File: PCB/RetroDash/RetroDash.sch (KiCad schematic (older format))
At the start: 4 parts

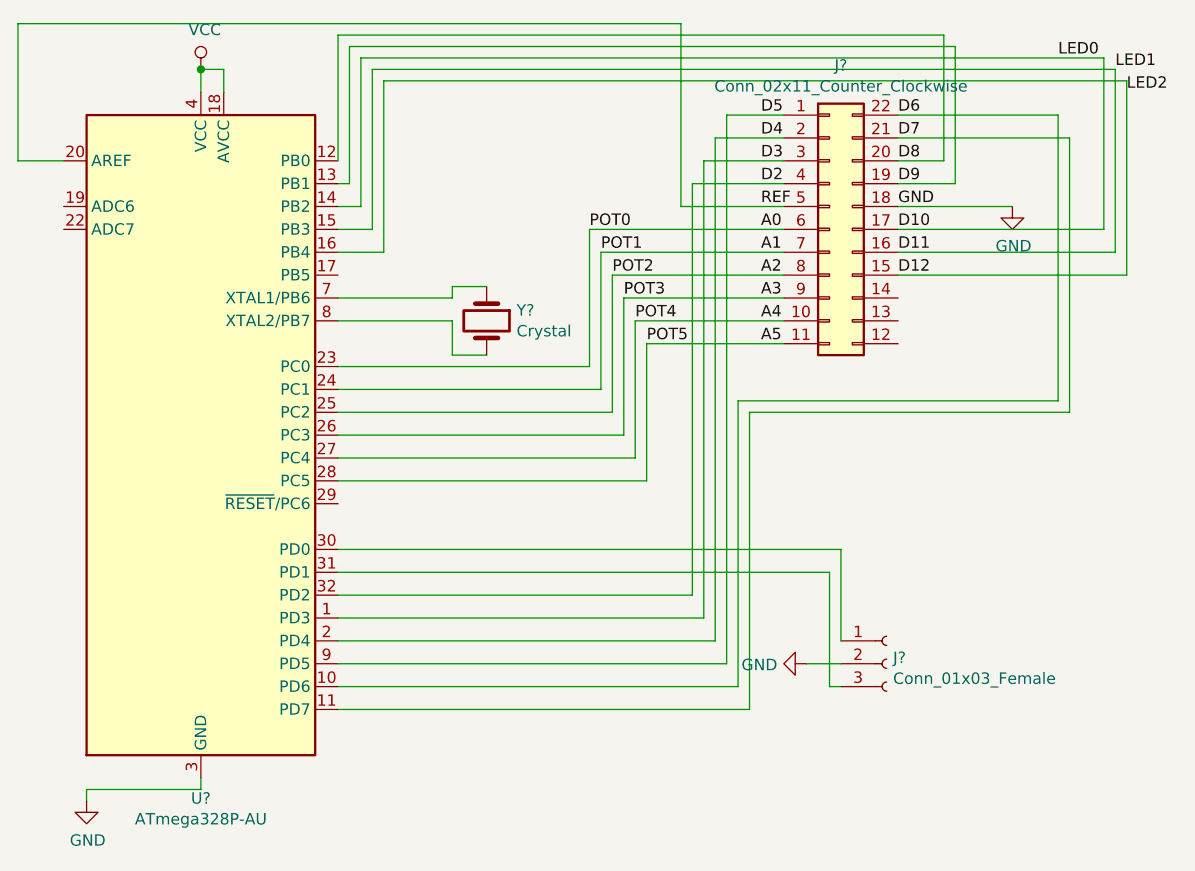
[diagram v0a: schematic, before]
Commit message: fixed nc pin
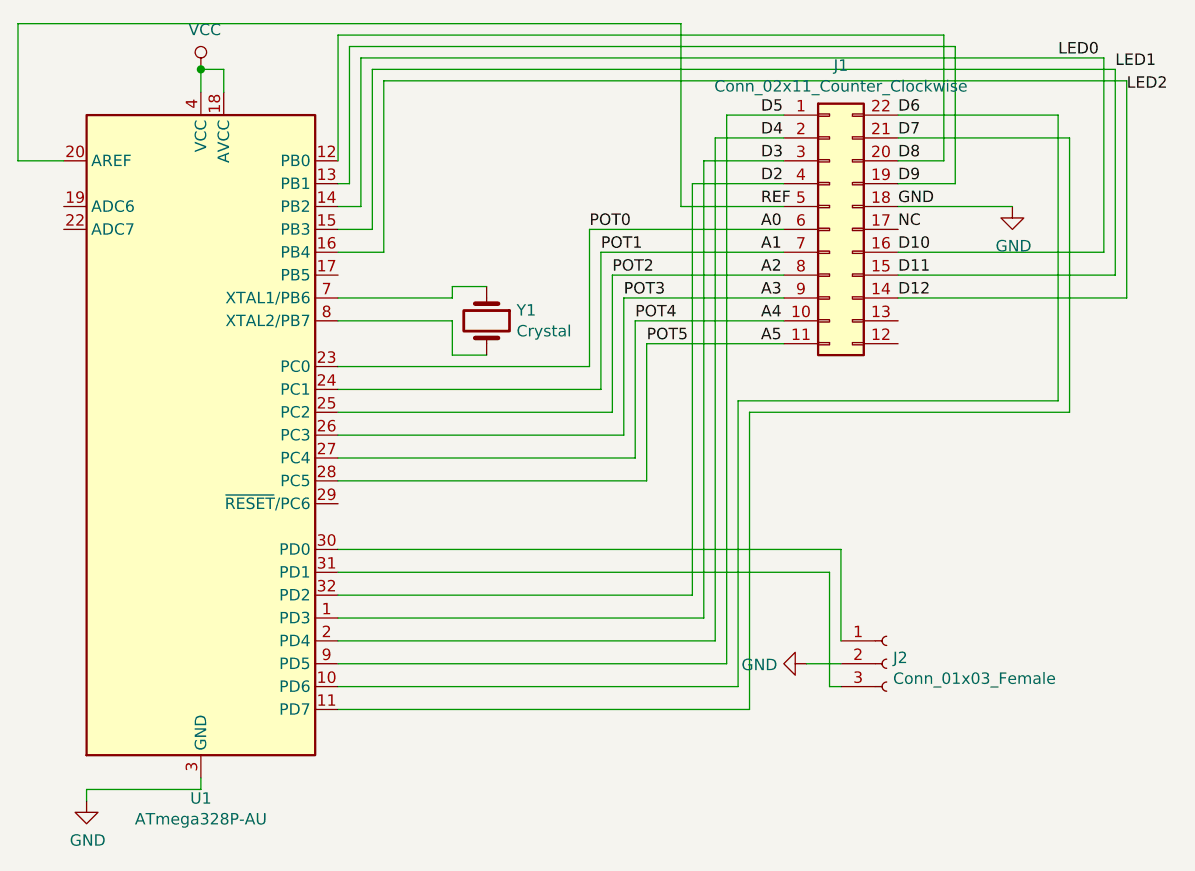
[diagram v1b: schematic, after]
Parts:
- gave numbers to parts that had none: 4
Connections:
- net D10: now also J1.16 (Pin_16); no longer J1.17 (Pin_17)
- net D11: now also J1.15 (Pin_15); no longer J1.16 (Pin_16)
- net D12: now also J1.14 (Pin_14); no longer J1.15 (Pin_15)
- new net NC: J1.17 (Pin_17)
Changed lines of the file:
@@
 EESchema Schematic File Version 4
+LIBS:RetroDash-cache
 EELAYER 29 0
 EELAYER END
@@
 $EndDescr
 $Comp
-L Connector_Generic:Conn_02x11_Counter_Clockwise J?
+L Connector_Generic:Conn_02x11_Counter_Clockwise J1
 U 1 1 5CB62158
 P 6600 1650
-F 0 "J?" H 6650 2367 50  0000 C CNN
+F 0 "J1" H 6650 2367 50  0000 C CNN
 F 1 "Conn_02x11_Counter_Clockwise" H 6650 2276 50  0000 C CNN
 F 2 "" H 6600 1650 50  0001 C CNN
@@
 	6900 1550 7400 1550
 $Comp
-L power:GND #PWR?
+L power:GND #PWR0101
 U 1 1 5CB6A467
 P 7400 1550
-F 0 "#PWR?" H 7400 1300 50  0001 C CNN
+F 0 "#PWR0101" H 7400 1300 50  0001 C CNN
 F 1 "GND" H 7405 1377 50  0000 C CNN
 F 2 "" H 7400 1550 50  0001 C CNN
@@
 $EndComp
 $Comp
-L power:GND #PWR?
+L power:GND #PWR0102
 U 1 1 5CB6B3B1
 P 3350 4150
-F 0 "#PWR?" H 3350 3900 50  0001 C CNN
+F 0 "#PWR0102" H 3350 3900 50  0001 C CNN
 F 1 "GND" H 3355 3977 50  0000 C CNN
 F 2 "" H 3350 4150 50  0001 C CNN
@@
 	5950 1550 6400 1550
 $Comp
-L power:VCC #PWR?
+L power:VCC #PWR0103
 U 1 1 5CB6F2DF
 P 3850 950
-F 0 "#PWR?" H 3850 800 50  0001 C CNN
+F 0 "#PWR0103" H 3850 800 50  0001 C CNN
 F 1 "VCC" H 3867 1123 50  0000 C CNN
 F 2 "" H 3850 950 50  0001 C CNN
@@
 	5800 2750 4450 2750
 $Comp
-L power:GND #PWR?
+L power:GND #PWR0104
 U 1 1 5CB77E47
 P 6500 3550
-F 0 "#PWR?" H 6500 3300 50  0001 C CNN
+F 0 "#PWR0104" H 6500 3300 50  0001 C CNN
 F 1 "GND" V 6505 3422 50  0000 R CNN
 F 2 "" H 6500 3550 50  0001 C CNN
@@
 	5950 750  5950 1550
 $Comp
-L Connector:Conn_01x03_Female J?
+L Connector:Conn_01x03_Female J2
 U 1 1 5CB74F2E
 P 6850 3550
-F 0 "J?" H 6878 3576 50  0000 L CNN
+F 0 "J2" H 6878 3576 50  0000 L CNN
 F 1 "Conn_01x03_Female" H 6878 3485 50  0000 L CNN
 F 2 "" H 6850 3550 50  0001 C CNN
@@
 $EndComp
 $Comp
-L Device:Crystal Y?
+L Device:Crystal Y1
 U 1 1 5CB70044
 P 5100 2050
-F 0 "Y?" V 5054 2181 50  0000 L CNN
+F 0 "Y1" V 5054 2181 50  0000 L CNN
 F 1 "Crystal" V 5145 2181 50  0000 L CNN
 F 2 "" H 5100 2050 50  0001 C CNN
@@
 	4450 1950 4950 1950
 $Comp
-L MCU_Microchip_ATmega:ATmega328P-AU U?
+L MCU_Microchip_ATmega:ATmega328P-AU U1
 U 1 1 5CB6371F
 P 3850 2550
-F 0 "U?" H 3850 961 50  0000 C CNN
+F 0 "U1" H 3850 961 50  0000 C CNN
 F 1 "ATmega328P-AU" H 3850 870 50  0000 C CNN
 F 2 "Package_QFP:TQFP-32_7x7mm_P0.8mm" H 3850 2550 50  0001 C CIN
@@
 	4550 900  7800 900
 Wire Wire Line
-	7800 900  7800 1650
-Wire Wire Line
-	7800 1650 6900 1650
-Wire Wire Line
 	4450 1650 4600 1650
 Wire Wire Line
@@
 	4600 950  7850 950
 Wire Wire Line
-	7850 950  7850 1750
-Wire Wire Line
-	7850 1750 6900 1750
-Wire Wire Line
 	4450 1750 4650 1750
 Wire Wire Line
@@
 Wire Wire Line
 	4650 1000 7900 1000
-Wire Wire Line
-	7900 1000 7900 1850
-Wire Wire Line
-	7900 1850 6900 1850
 Text Label 7600 900  0    50   ~ 0
 LED0
@@
 Text Label 6900 1550 0    50   ~ 0
 GND
-Text Label 6900 1650 0    50   ~ 0
+Text Label 6900 1750 0    50   ~ 0
 D10
-Text Label 6900 1750 0    50   ~ 0
+Text Label 6900 1850 0    50   ~ 0
 D11
-Text Label 6900 1850 0    50   ~ 0
+Text Label 6900 1950 0    50   ~ 0
 D12
 Wire Wire Line
@@
 	3050 750  5950 750
 Connection ~ 3850 950
+Wire Wire Line
+	7800 1750 6900 1750
+Wire Wire Line
+	7800 900  7800 1750
+Wire Wire Line
+	7850 1850 6900 1850
+Wire Wire Line
+	7850 950  7850 1850
+Wire Wire Line
+	7900 1950 6900 1950
+Wire Wire Line
+	7900 1000 7900 1950
+Text Label 6900 1650 0    50   ~ 0
+NC
 $EndSCHEMATC
